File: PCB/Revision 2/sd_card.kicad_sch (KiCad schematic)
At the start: 8 parts, among them J3 SD_Card

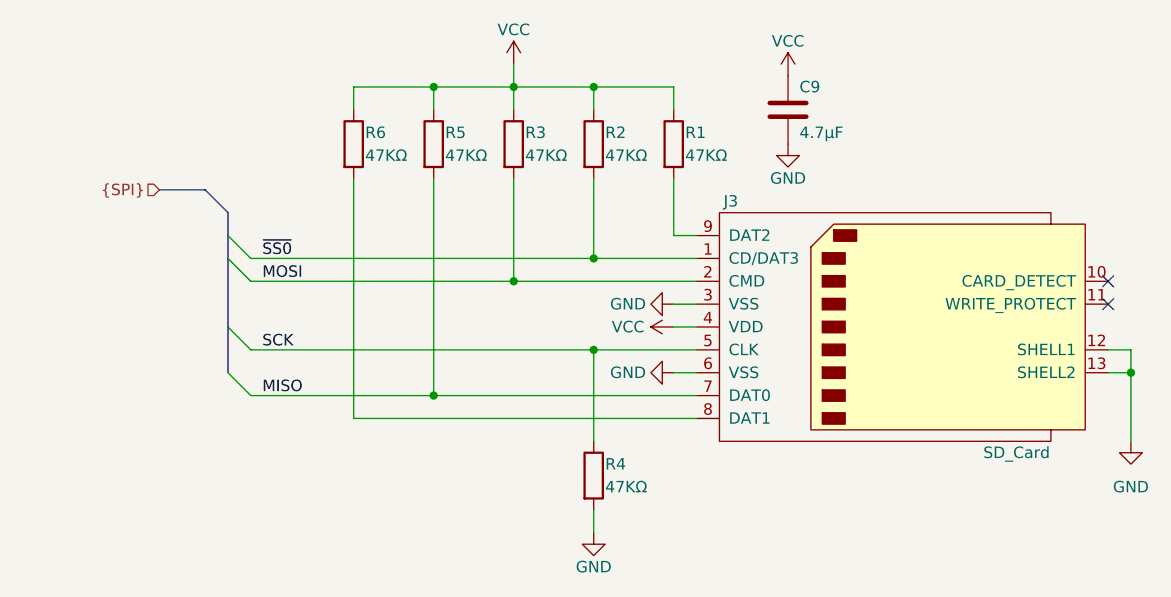
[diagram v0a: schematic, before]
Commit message: ESD protection diodes go BRRRRRRR
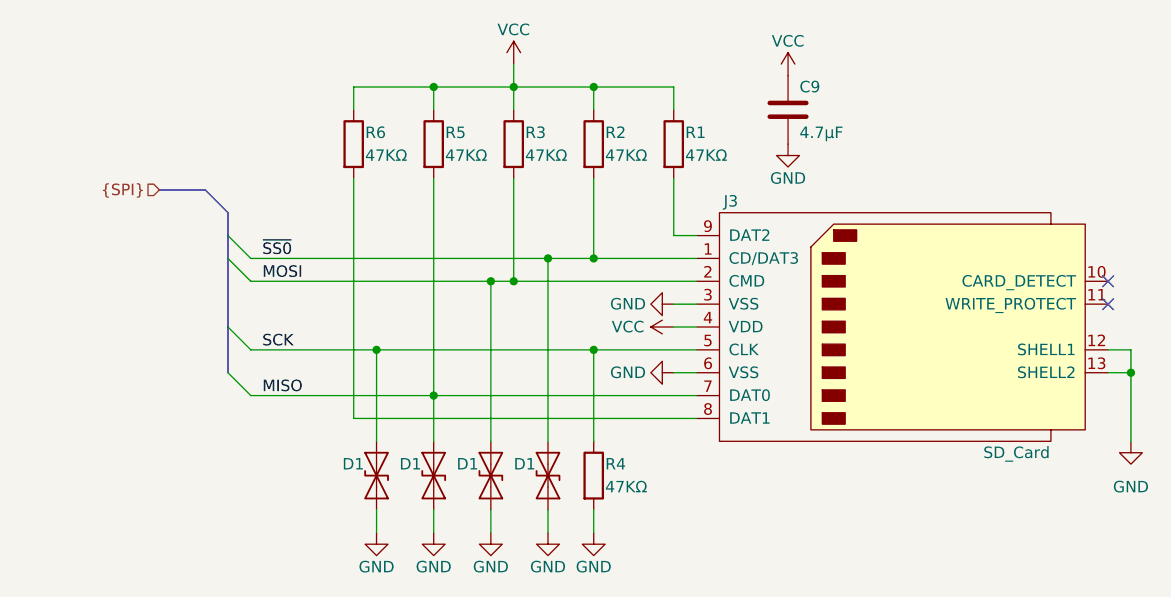
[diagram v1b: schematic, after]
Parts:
- added D1 (x4): ESD9B3.3ST5G, Diode_SMD:D_SOD-923, symbol Diode:ESD9B3.3ST5G
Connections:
- net GND: now also D1.2 (A2), D1.2 (A2), D1.2 (A2), D1.2 (A2)
- net MISO: now also D1.1 (A1)
- net MOSI: now also D1.1 (A1)
- net SCK: now also D1.1 (A1)
- net ~{SS0}: now also D1.1 (A1)

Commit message: Updated re: issue #2
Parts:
- added R3: 10Ω, symbol Device:R
- C9: footprint (none) -> Capacitor_SMD:C_0402_1005Metric
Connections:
- net MISO: now also R3.2; no longer D1.1 (A1), J3.7 (DAT0), R5.2
- new net: D1.1 (A1), J3.7 (DAT0), R3.1, R5.2
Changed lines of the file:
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@@
   (no_connect (at 198.12 101.6))
   (no_connect (at 198.12 104.14))
-  (bus_entry (at 100.33 99.06) (size 2.54 2.54)
-    (stroke (width 0) (type default))
-  )
-  (bus_entry (at 100.33 111.76) (size 2.54 2.54)
-    (stroke (width 0) (type default))
-  )
-  (bus_entry (at 100.33 96.52) (size 2.54 2.54)
-    (stroke (width 0) (type default))
-  )
-  (bus_entry (at 100.33 106.68) (size 2.54 2.54)
+  (bus_entry (at 92.71 99.06) (size 2.54 2.54)
+    (stroke (width 0) (type default))
+  )
+  (bus_entry (at 92.71 111.76) (size 2.54 2.54)
+    (stroke (width 0) (type default))
+  )
+  (bus_entry (at 92.71 96.52) (size 2.54 2.54)
+    (stroke (width 0) (type default))
+  )
+  (bus_entry (at 92.71 106.68) (size 2.54 2.54)
     (stroke (width 0) (type default))
   )
@@
     (stroke (width 0) (type default))
   )
+  (wire (pts (xy 95.25 109.22) (xy 116.84 109.22))
+    (stroke (width 0) (type default))
+  )
   (wire (pts (xy 129.54 127) (xy 129.54 129.54))
     (stroke (width 0) (type default))
   )
+  (wire (pts (xy 111.76 114.3) (xy 123.19 114.3))
+    (stroke (width 0) (type default))
+  )
   (wire (pts (xy 135.89 99.06) (xy 135.89 119.38))
     (stroke (width 0) (type default))
@@
     (stroke (width 0) (type default))
   )
+  (wire (pts (xy 95.25 99.06) (xy 135.89 99.06))
+    (stroke (width 0) (type default))
+  )
   (wire (pts (xy 149.86 90.17) (xy 149.86 96.52))
     (stroke (width 0) (type default))
@@
     (stroke (width 0) (type default))
   )
-  (bus (pts (xy 100.33 99.06) (xy 100.33 106.68))
-    (stroke (width 0) (type default))
-  )
-  (bus (pts (xy 100.33 93.98) (xy 100.33 96.52))
+  (bus (pts (xy 92.71 99.06) (xy 92.71 106.68))
+    (stroke (width 0) (type default))
+  )
+  (bus (pts (xy 92.71 93.98) (xy 92.71 96.52))
     (stroke (width 0) (type default))
   )
@@
     (stroke (width 0) (type default))
   )
-  (wire (pts (xy 102.87 114.3) (xy 123.19 114.3))
-    (stroke (width 0) (type default))
-  )
   (wire (pts (xy 116.84 109.22) (xy 140.97 109.22))
     (stroke (width 0) (type default))
@@
     (stroke (width 0) (type default))
   )
-  (wire (pts (xy 102.87 99.06) (xy 135.89 99.06))
-    (stroke (width 0) (type default))
-  )
-  (wire (pts (xy 102.87 101.6) (xy 129.54 101.6))
-    (stroke (width 0) (type default))
-  )
-  (bus (pts (xy 100.33 96.52) (xy 100.33 99.06))
+  (wire (pts (xy 95.25 101.6) (xy 129.54 101.6))
+    (stroke (width 0) (type default))
+  )
+  (bus (pts (xy 92.71 96.52) (xy 92.71 99.06))
     (stroke (width 0) (type default))
   )
@@
     (stroke (width 0) (type default))
   )
-  (bus (pts (xy 97.79 91.44) (xy 100.33 93.98))
+  (bus (pts (xy 90.17 91.44) (xy 92.71 93.98))
     (stroke (width 0) (type default))
   )
@@
     (stroke (width 0) (type default))
   )
-  (wire (pts (xy 102.87 109.22) (xy 116.84 109.22))
-    (stroke (width 0) (type default))
-  )
-  (bus (pts (xy 92.71 91.44) (xy 97.79 91.44))
+  (bus (pts (xy 85.09 91.44) (xy 90.17 91.44))
     (stroke (width 0) (type default))
   )
@@
     (stroke (width 0) (type default))
   )
-  (bus (pts (xy 100.33 106.68) (xy 100.33 111.76))
+  (bus (pts (xy 92.71 106.68) (xy 92.71 111.76))
     (stroke (width 0) (type default))
   )
@@
     (stroke (width 0) (type default))
   )
+  (wire (pts (xy 95.25 114.3) (xy 104.14 114.3))
+    (stroke (width 0) (type default))
+  )
   (wire (pts (xy 140.97 80.01) (xy 140.97 82.55))
     (stroke (width 0) (type default))
   )
-  (label "~{SS0}" (at 104.14 99.06 0) (fields_autoplaced)
+  (label "~{SS0}" (at 96.52 99.06 0) (fields_autoplaced)
     (effects (font (size 1.27 1.27)) (justify left bottom))
   )
-  (label "MOSI" (at 104.14 101.6 0) (fields_autoplaced)
+  (label "MOSI" (at 96.52 101.6 0) (fields_autoplaced)
     (effects (font (size 1.27 1.27)) (justify left bottom))
   )
-  (label "MISO" (at 104.14 114.3 0) (fields_autoplaced)
+  (label "MISO" (at 96.52 114.3 0) (fields_autoplaced)
     (effects (font (size 1.27 1.27)) (justify left bottom))
   )
-  (label "SCK" (at 104.14 109.22 0) (fields_autoplaced)
+  (label "SCK" (at 96.52 109.22 0) (fields_autoplaced)
     (effects (font (size 1.27 1.27)) (justify left bottom))
   )
-  (hierarchical_label "{SPI}" (shape input) (at 92.71 91.44 180) (fields_autoplaced)
+  (hierarchical_label "{SPI}" (shape input) (at 85.09 91.44 180) (fields_autoplaced)
     (effects (font (size 1.27 1.27)) (justify right))
   )
@@
         (path "/3ba39048-ccb5-49b6-bc29-f9a8dd2e53b6/ef7f0437-b22e-4c24-9273-d90d53267996"
           (reference "#PWR0152") (unit 1)
+        )
+      )
+    )
+  )
+  (symbol (lib_id "Device:R") (at 107.95 114.3 270) (unit 1)
+    (in_bom yes) (on_board yes) (dnp no)
+    (property "Reference" "R3" (at 107.95 111.76 90)
+      (effects (font (size 1.27 1.27)))
+    )
+    (property "Value" "10Ω" (at 107.95 114.3 90)
+      (effects (font (size 1.27 1.27)))
+    )
+    (property "Footprint" "" (at 107.95 112.522 90)
+      (effects (font (size 1.27 1.27)) hide)
+    )
+    (property "Datasheet" "~" (at 107.95 114.3 0)
+      (effects (font (size 1.27 1.27)) hide)
+    )
+    (pin "1")
+    (pin "2")
+    (instances
+      (project "Revision 2"
+        (path "/3ba39048-ccb5-49b6-bc29-f9a8dd2e53b6/ef7f0437-b22e-4c24-9273-d90d53267996"
+          (reference "R3") (unit 1)
         )
       )
@@
       (effects (font (size 1.27 1.27)) (justify left))
     )
-    (property "Footprint" "" (at 163.5252 86.36 0)
-      (effects (font (size 1.27 1.27)) hide)
-    )
+    (property "Footprint" "Capacitor_SMD:C_0402_1005Metric" (at 163.5252 86.36 0)
+      (effects (font (size 1.27 1.27)) hide)
+    )
